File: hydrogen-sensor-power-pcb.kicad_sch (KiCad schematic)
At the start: 32 parts, among them U4 TPS62933, U9 TPS62933

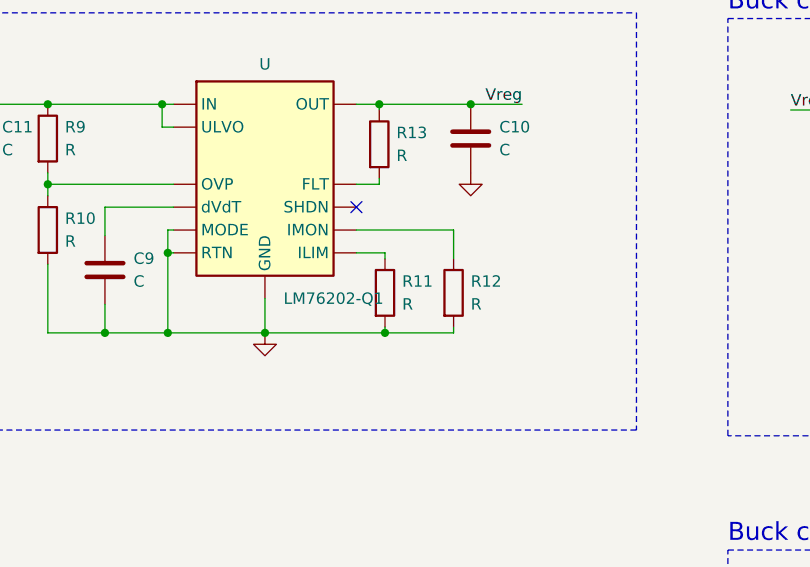
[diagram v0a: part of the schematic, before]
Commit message: Finish Vcc configuration and add USB-C
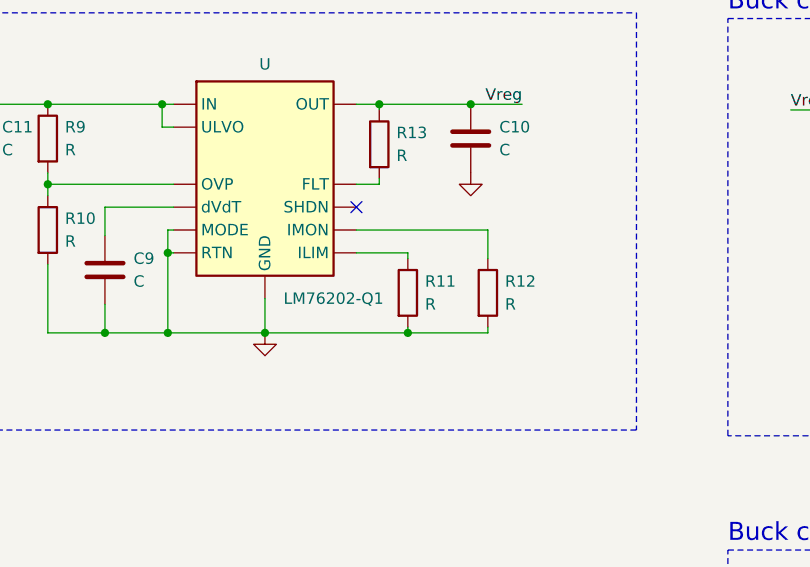
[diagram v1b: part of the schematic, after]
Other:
- moved on the sheet: R11, R12
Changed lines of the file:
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@@
   (junction (at 66.04 60.325) (diameter 0) (color 0 0 0 0)
   )
-  (junction (at 111.76 85.725) (diameter 0) (color 0 0 0 0)
+  (junction (at 114.3 85.725) (diameter 0) (color 0 0 0 0)
   )
   (junction (at 98.425 85.725) (diameter 0) (color 0 0 0 0)
@@
   )
   (no_connect (at 108.585 71.755))
-  (wire (pts (xy 111.76 85.725) (xy 119.38 85.725))
+  (wire (pts (xy 114.3 85.725) (xy 123.19 85.725))
     (stroke (width 0) (type default))
   )
@@
     (stroke (width 0) (type default))
   )
-  (wire (pts (xy 108.585 76.835) (xy 111.76 76.835))
-    (stroke (width 0) (type default))
-  )
-  (wire (pts (xy 111.76 85.725) (xy 98.425 85.725))
+  (wire (pts (xy 108.585 76.835) (xy 114.3 76.835))
+    (stroke (width 0) (type default))
+  )
+  (wire (pts (xy 114.3 85.725) (xy 98.425 85.725))
     (stroke (width 0) (type default))
   )
@@
     (stroke (width 0) (type default))
   )
-  (wire (pts (xy 111.76 85.725) (xy 111.76 85.09))
+  (wire (pts (xy 114.3 85.725) (xy 114.3 85.09))
     (stroke (width 0) (type default))
   )
@@
     (stroke (width 0) (type default))
   )
-  (wire (pts (xy 119.38 85.725) (xy 119.38 85.09))
+  (wire (pts (xy 123.19 85.725) (xy 123.19 85.09))
     (stroke (width 0) (type default))
   )
@@
     (stroke (width 0) (type default))
   )
-  (wire (pts (xy 119.38 74.295) (xy 108.585 74.295))
+  (wire (pts (xy 123.19 74.295) (xy 108.585 74.295))
     (stroke (width 0) (type default))
   )
@@
     (stroke (width 0) (type default))
   )
-  (wire (pts (xy 111.76 76.835) (xy 111.76 77.47))
+  (wire (pts (xy 114.3 76.835) (xy 114.3 77.47))
     (stroke (width 0) (type default))
   )
@@
     (stroke (width 0) (type default))
   )
-  (wire (pts (xy 119.38 77.47) (xy 119.38 74.295))
+  (wire (pts (xy 123.19 77.47) (xy 123.19 74.295))
     (stroke (width 0) (type default))
   )
@@
     )
   )
-  (symbol (lib_id "Device:R") (at 119.38 81.28 0) (unit 1)
-    (in_bom yes) (on_board yes) (dnp no) (fields_autoplaced)
-    (property "Reference" "R12" (at 121.285 80.0099 0)
-      (effects (font (size 1.27 1.27)) (justify left))
-    )
-    (property "Value" "R" (at 121.285 82.5499 0)
-      (effects (font (size 1.27 1.27)) (justify left))
-    )
-    (property "Footprint" "" (at 117.602 81.28 90)
-      (effects (font (size 1.27 1.27)) hide)
-    )
-    (property "Datasheet" "~" (at 119.38 81.28 0)
+  (symbol (lib_id "Device:R") (at 123.19 81.28 0) (unit 1)
+    (in_bom yes) (on_board yes) (dnp no) (fields_autoplaced)
+    (property "Reference" "R12" (at 125.095 80.0099 0)
+      (effects (font (size 1.27 1.27)) (justify left))
+    )
+    (property "Value" "R" (at 125.095 82.5499 0)
+      (effects (font (size 1.27 1.27)) (justify left))
+    )
+    (property "Footprint" "" (at 121.412 81.28 90)
+      (effects (font (size 1.27 1.27)) hide)
+    )
+    (property "Datasheet" "~" (at 123.19 81.28 0)
       (effects (font (size 1.27 1.27)) hide)
     )
@@
     )
   )
-  (symbol (lib_id "Device:R") (at 111.76 81.28 0) (unit 1)
-    (in_bom yes) (on_board yes) (dnp no) (fields_autoplaced)
-    (property "Reference" "R11" (at 113.665 80.0099 0)
-      (effects (font (size 1.27 1.27)) (justify left))
-    )
-    (property "Value" "R" (at 113.665 82.5499 0)
-      (effects (font (size 1.27 1.27)) (justify left))
-    )
-    (property "Footprint" "" (at 109.982 81.28 90)
-      (effects (font (size 1.27 1.27)) hide)
-    )
-    (property "Datasheet" "~" (at 111.76 81.28 0)
-      (effects (font (size 1.27 1.27)) hide)
-    )
+  (symbol (lib_id "Device:R") (at 114.3 81.28 0) (unit 1)
+    (in_bom yes) (on_board yes) (dnp no) (fields_autoplaced)
+    (property "Reference" "R11" (at 116.205 80.0099 0)
+      (effects (font (size 1.27 1.27)) (justify left))
+    )
+    (property "Value" "R" (at 116.205 82.5499 0)
+      (effects (font (size 1.27 1.27)) (justify left))
+    )
+    (property "Footprint" "" (at 112.522 81.28 90)
+      (effects (font (size 1.27 1.27)) hide)
+    )
+    (property "Datasheet" "~" (at 114.3 81.28 0)
+      (effects (font (size 1.27 1.27)) hide)
+    )
